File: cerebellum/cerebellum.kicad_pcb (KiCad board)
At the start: 4 copper layers, 91.5 x 52 mm, 82 parts, among them J1 PowerIn, J2 UART, J3 SWD_DBG, J4 SWD_DBG_PIN, J5 PowerOut, J6 CAN, Q1 AP2300, U1 OK1061-S, U2 TPS5430DDA, U3 BMI088, U4 TJA1042T, U5 ICP-20100, U6 TJA1042T, U7 TPS54231

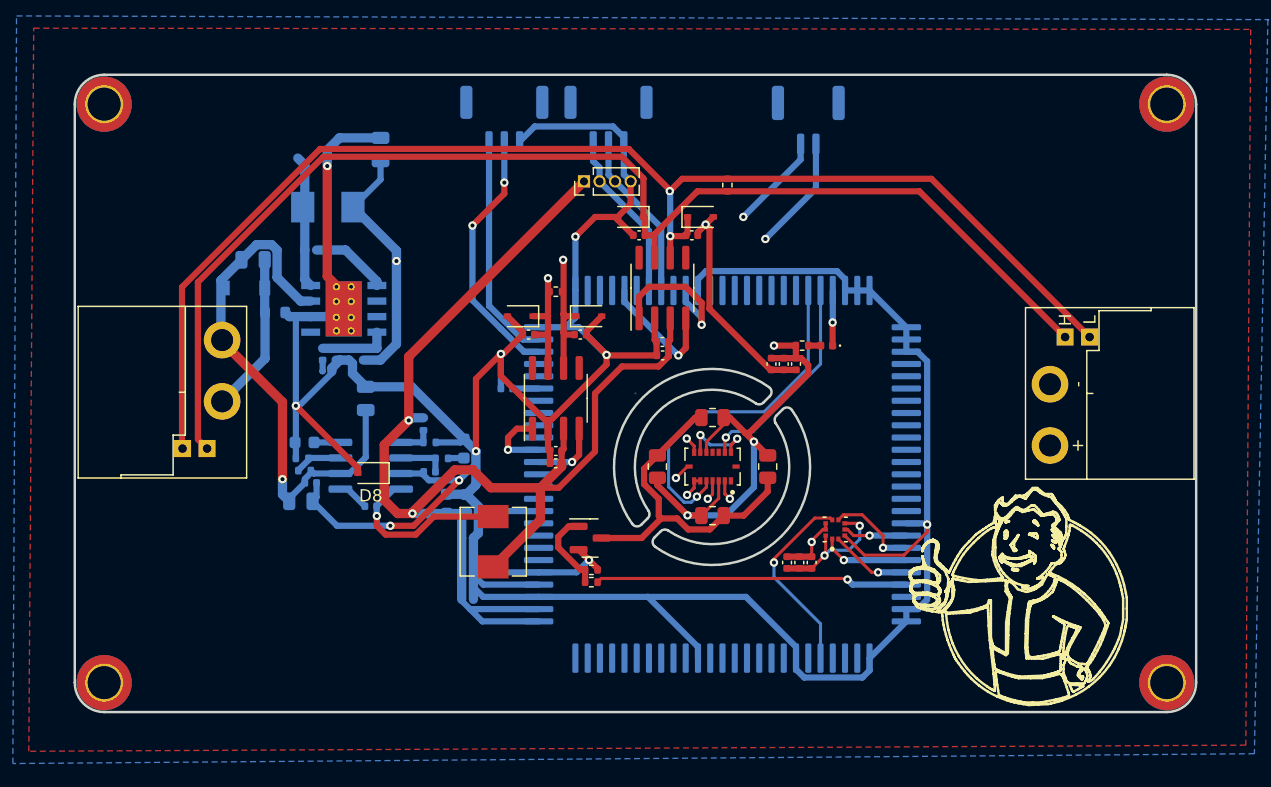
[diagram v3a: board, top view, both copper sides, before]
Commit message: [New] Rerouting cerebellum & add dxfs
1. Rerouting cerebellum for new design. There are only two layers in this design.
2. Add common board DXF file and cerebellum DXF file. Also I added their source file for convenient modification in the future.
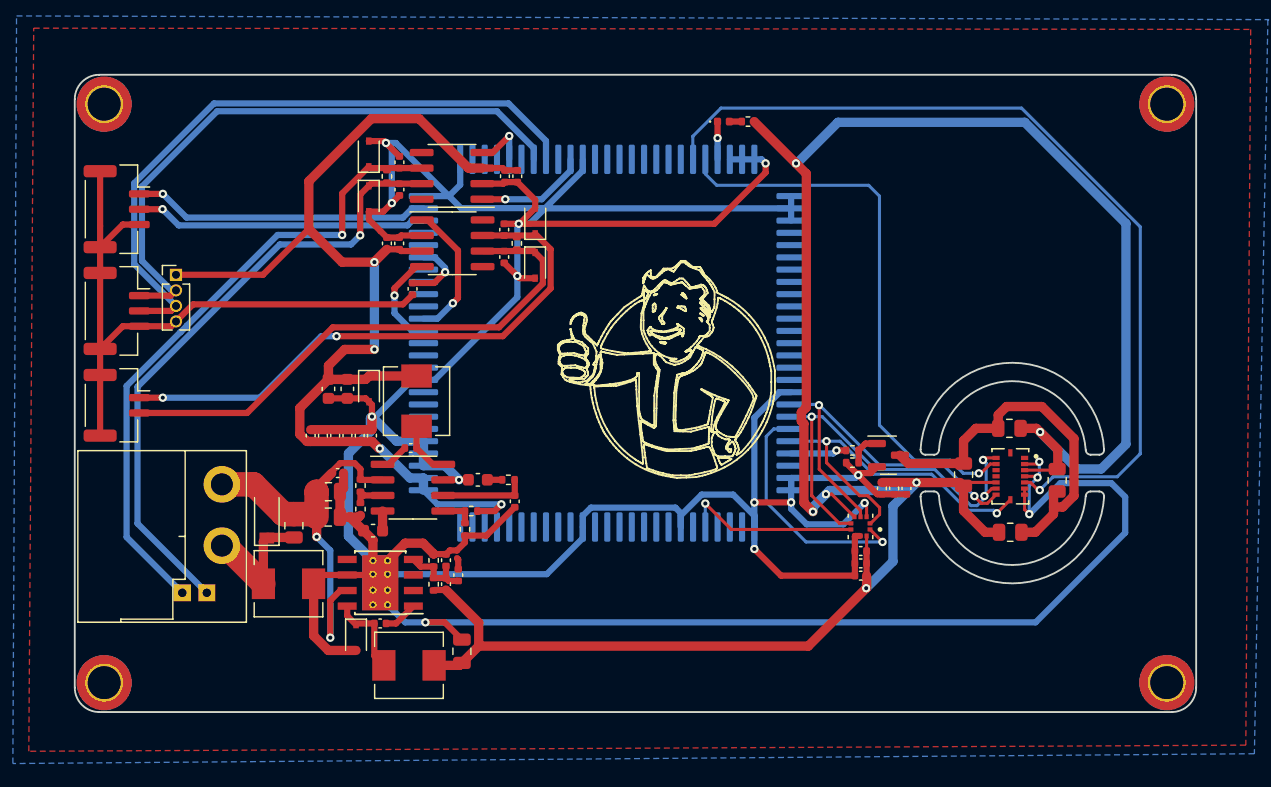
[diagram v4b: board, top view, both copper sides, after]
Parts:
- removed FB1: 220R, Resistor_SMD:R_0603_1608Metric
- removed J5: PowerOut, Rolling_Custom:XT30PW(2+2)
- added L3: 15uh, SLO0530H150MTT, Inductor_SMD:L_Sunlord_MWSA0518_5.4x5.2mm, F.Cu at (121.7, 115.5)
- C1, C13, C14, C15, C16, C17, C18, C19, C2, C21, C24, C25, C26, C27, C28, C3, C33, C36, C38, C4, C5, C6, D1, D2, J2, J4, L2, R11, R16, R17, R3, R4, R5, R6, R7, U2, U7: moved to F.Cu
- J6: footprint Connector_JST:JST_GH_BM02B-GHS-TBT_1x02-1MP_P1.25mm_Vertical -> Connector_JST:JST_GH_SM02B-GHS-TB_1x02-1MP_P1.25mm_Horizontal; moved to F.Cu
- moved J1 68.6 mm to (116.3, 111.7), turned to -90 degrees
- moved J6 61.0 mm to (107.7, 101.0), turned to -90 degrees
- moved J4 43.1 mm to (107.7, 93.3), turned to -90 degrees
- moved C19 41.5 mm to (135.8, 121.0)
- moved D2 39.3 mm to (127.2, 119.9), turned to -90 degrees
- moved L2 38.0 mm to (131.5, 122.2)
- moved J3 34.2 mm to (112.5, 90.3), turned to 0 degrees
- moved J2 32.5 mm to (107.7, 85.0), turned to -90 degrees
- moved C17 31.0 mm to (129.2, 118.8)
- moved R12 28.9 mm to (180.5, 102.8), turned to 180 degrees
- moved R13 28.3 mm to (184.4, 107.1), turned to -90 degrees
- moved R2 27.8 mm to (129.7, 82.3)
- moved D6 27.5 mm to (128.2, 80.5), turned to 90 degrees
- moved R14 26.0 mm to (180.6, 111.3), turned to 0 degrees
- moved Q1 25.3 mm to (170.6, 105.0)
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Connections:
- J2 pad MP: (no net) -> GND
- J4 pad MP: (no net) -> GND
- J6 pad MP: (no net) -> GND
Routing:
- net +24V: track 149.8 -> 32.8 mm, vias 1 -> 2
- net GNDA: track 107.0 -> 10.7 mm
- net +3V3: track 128.5 -> 188.1 mm
- net GND: track 378.8 -> 435.7 mm, vias 15 -> 16
- net CANFD_L: track 107.2 -> 52.3 mm, vias 2 -> 1
- net CANFD_H: track 102.4 -> 51.2 mm, vias 0 -> 1
- net GYRO_SCS: track 28.3 -> 72.8 mm
- net SWCLK: track 13.9 -> 53.7 mm
- net SWDIO: track 14.0 -> 49.7 mm
- net ACC_SCS: track 17.5 -> 46.3 mm
- net BMI_HEAT: track 25.5 -> 4.59 mm
- net +5V: track 108.1 -> 94.8 mm, vias 2 -> 4
- net ICP_SCS: track 7.21 -> 19.9 mm
- net Net-(C27-Pad1): track 14.6 -> 4.50 mm, vias 1 -> 0
- net CAN_L: track 34.9 -> 44.4 mm, vias 2 -> 0
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- removed copper zone on In1.Cu, net +3V3
- removed copper zone on In2.Cu, net +5V
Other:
- outline, holes or cut-outs redrawn
- copper layers 4 -> 2

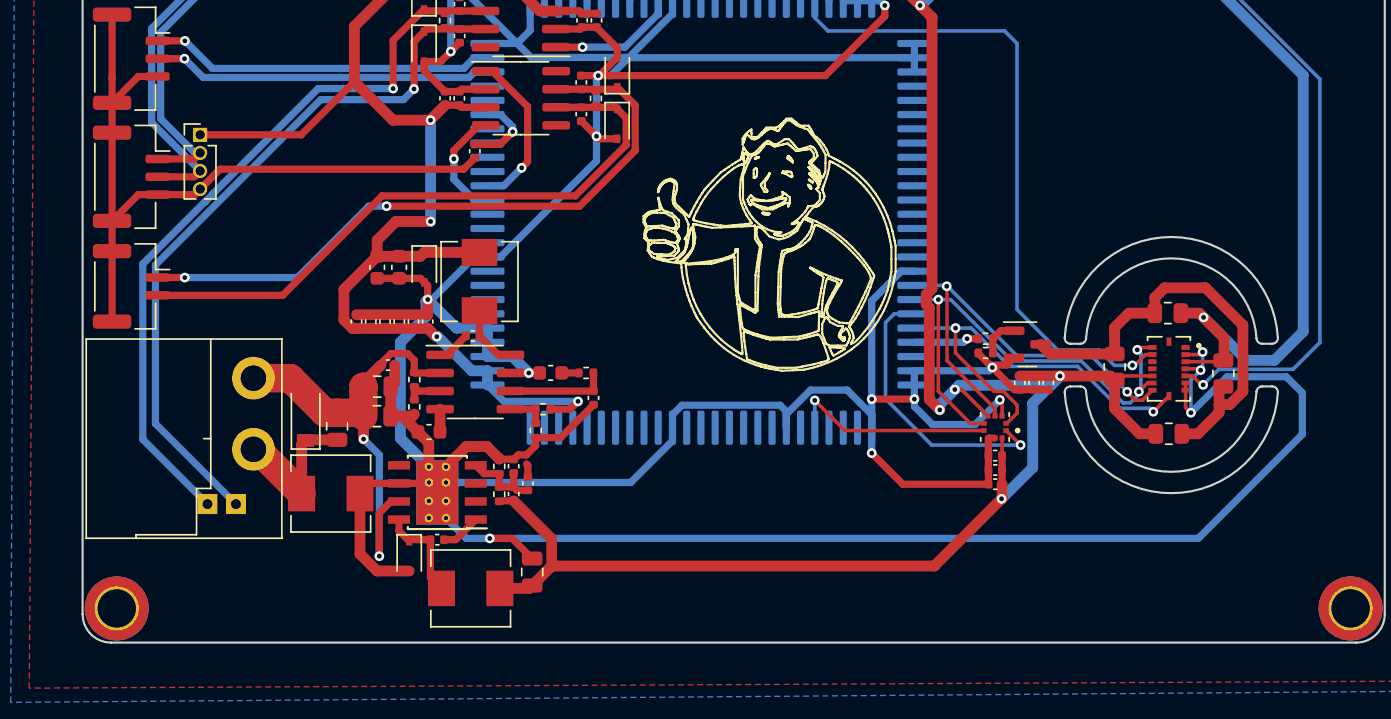
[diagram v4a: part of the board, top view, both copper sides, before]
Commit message: [Modify] Change XT30(2+2) input to XT30 + GH 2pin
As commit before.
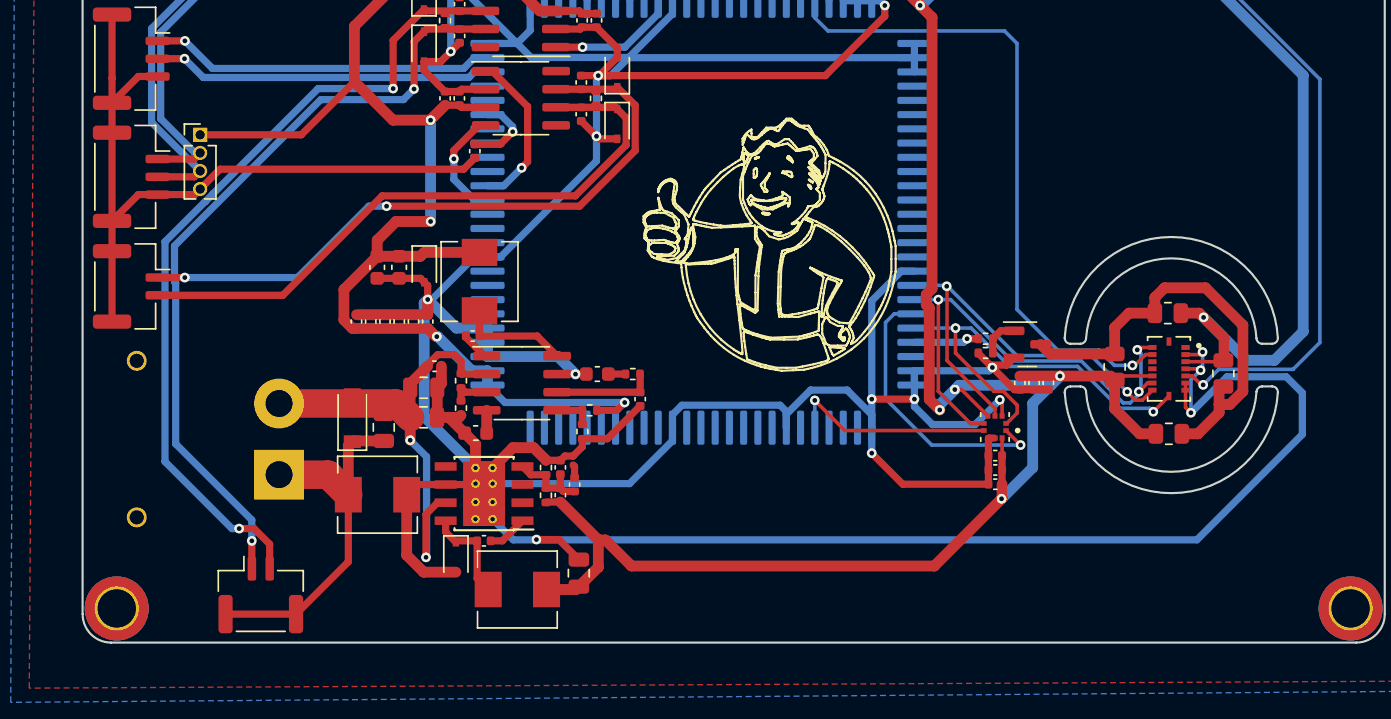
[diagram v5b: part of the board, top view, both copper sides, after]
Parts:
- added J5: CAN FD, Connector_JST:JST_GH_SM02B-GHS-TB_1x02-1MP_P1.25mm_Horizontal, F.Cu at (116.8, 122.7)
- J1: footprint Rolling_Custom:XT30PW(2+2) -> Connector_AMASS:AMASS_XT30PW-M_1x02_P2.50mm_Horizontal; moved to B.Cu
- moved C13 3.28 mm to (125.4, 110.9)
- moved C14 3.28 mm to (143.4, 108.9)
- moved C15 3.28 mm to (140.4, 107.1)
- moved C16 3.28 mm to (128.2, 110.2)
- moved C17 3.28 mm to (132.4, 118.8)
- moved C18 3.28 mm to (128.2, 108.1)
- moved C19 3.28 mm to (139.1, 121.1)
- moved C21 3.28 mm to (137.8, 115.6)
- moved C24 3.28 mm to (138.8, 114.9)
- moved C26 3.28 mm to (131.9, 111.3)
- moved C28 3.28 mm to (137.8, 113.7)
- moved D1 3.28 mm to (123.2, 110.2)
- moved L2 3.28 mm to (134.8, 122.3)
- moved L3 3.28 mm to (125.0, 115.6)
- moved R11 3.28 mm to (138.7, 113.2)
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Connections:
- J1 pad 1: +24V -> GNDA
- J1 pad 2: GNDA -> +24V
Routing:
- net GNDA: track 10.7 -> 26.4 mm
- net CANFD_L: track 52.3 -> 58.2 mm, vias 1 -> 2
- net CANFD_H: track 51.2 -> 55.0 mm, vias 1 -> 2
- net +5V: track 94.8 -> 98.1 mm
- net Net-(C27-Pad1): track 4.50 -> 7.82 mm
- net GND: track 435.7 -> 432.6 mm
- net +3V3: track 188.1 -> 185.6 mm
- net +24V: track 32.8 -> 34.0 mm

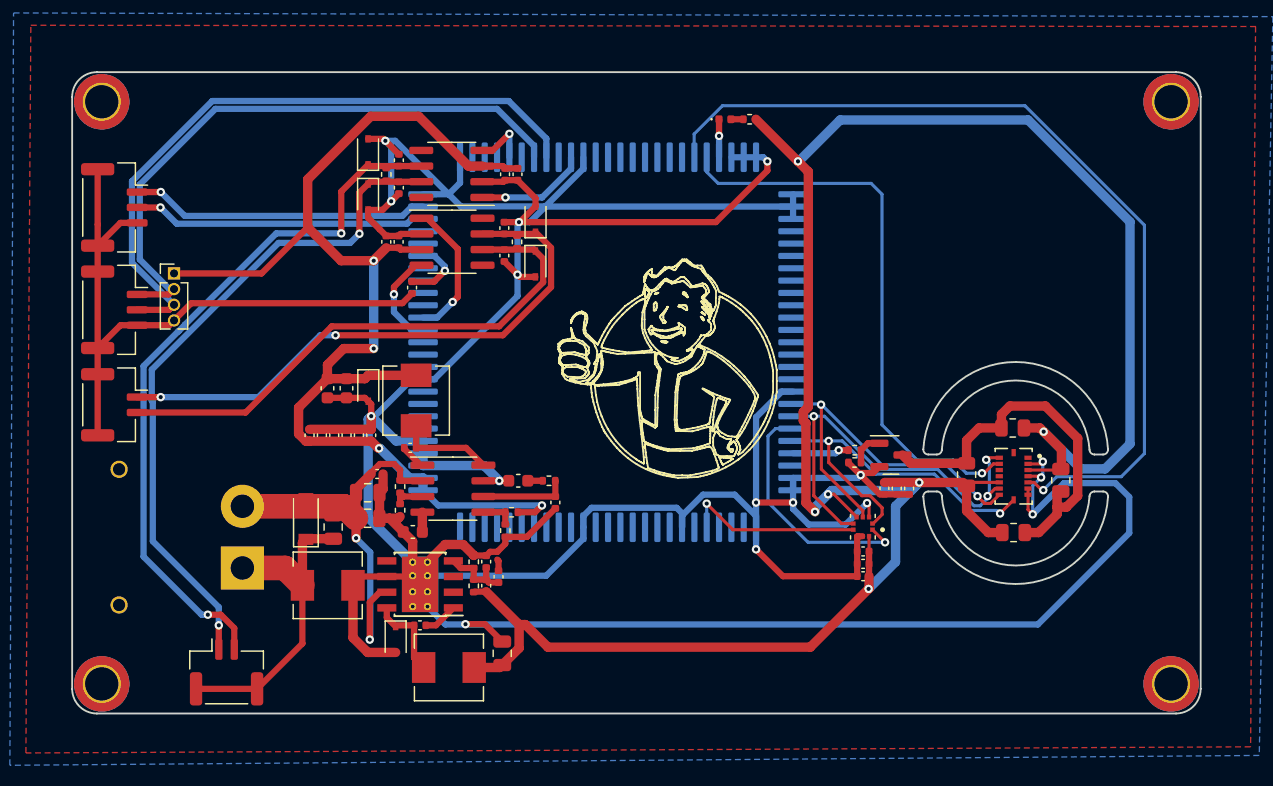
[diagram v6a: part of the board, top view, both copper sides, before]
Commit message: [Fix] Correct mounting hole positions
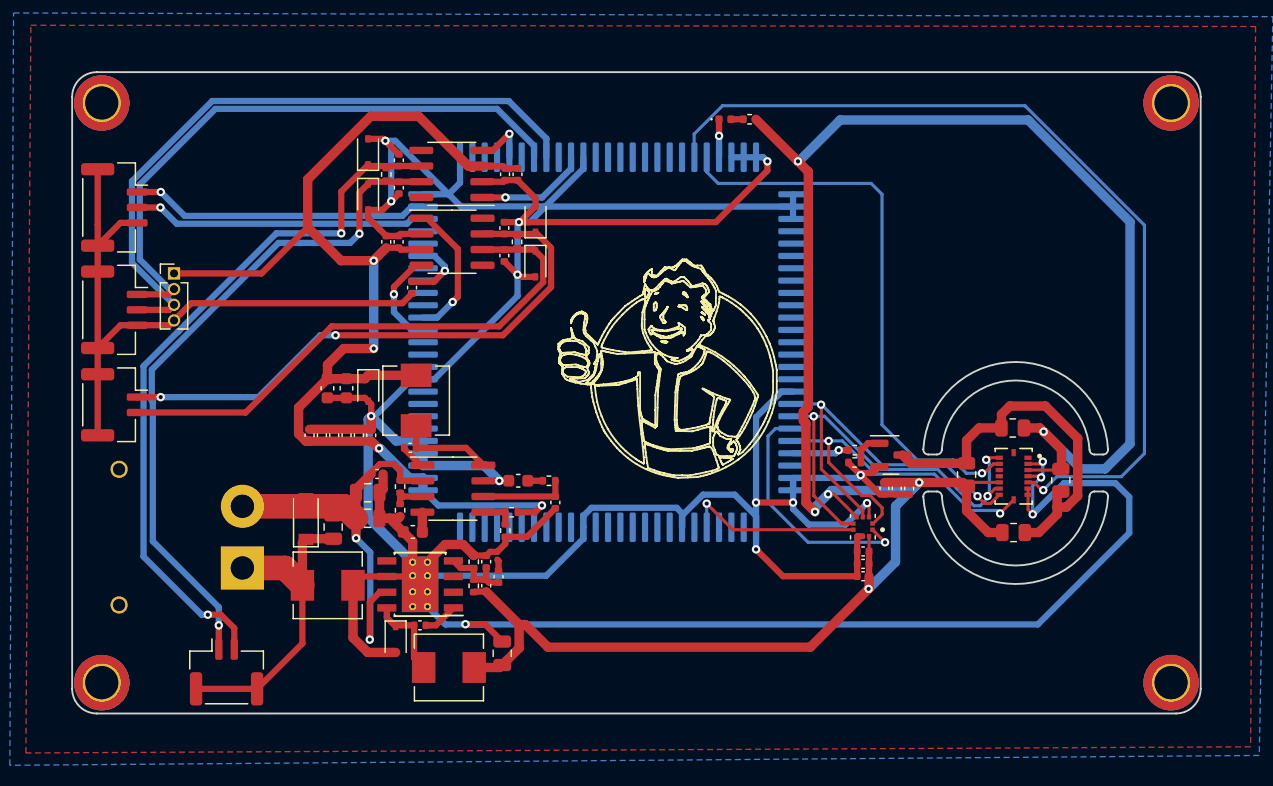
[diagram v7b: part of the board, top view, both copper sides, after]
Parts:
- moved Mount1 0.10 mm to (106.7, 76.5)
- moved Mount2 0.10 mm to (193.3, 76.5)
- moved Mount3 0.10 mm to (193.3, 123.5)
- moved Mount4 0.10 mm to (106.7, 123.5)
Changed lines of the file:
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@@
   )
   (footprint "MountingHole:MountingHole_2.7mm_M2.5_ISO7380_Pad_TopBottom" (layer "F.Cu")
-    (at 106.65 76.4)
+    (at 106.65 76.5)
     (descr "Mounting Hole 2.7mm, M2.5, ISO7380")
     (tags "mounting hole 2.7mm m2.5 iso7380")
@@
   )
   (footprint "MountingHole:MountingHole_2.7mm_M2.5_ISO7380_Pad_TopBottom" (layer "F.Cu")
-    (at 106.65 123.6)
+    (at 106.65 123.5)
     (descr "Mounting Hole 2.7mm, M2.5, ISO7380")
     (tags "mounting hole 2.7mm m2.5 iso7380")
@@
   )
   (footprint "MountingHole:MountingHole_2.7mm_M2.5_ISO7380_Pad_TopBottom" (layer "F.Cu")
-    (at 193.35 123.6)
+    (at 193.35 123.5)
     (descr "Mounting Hole 2.7mm, M2.5, ISO7380")
     (tags "mounting hole 2.7mm m2.5 iso7380")
@@
   )
   (footprint "MountingHole:MountingHole_2.7mm_M2.5_ISO7380_Pad_TopBottom" (layer "F.Cu")
-    (at 193.35 76.4)
+    (at 193.35 76.5)
     (descr "Mounting Hole 2.7mm, M2.5, ISO7380")
     (tags "mounting hole 2.7mm m2.5 iso7380")

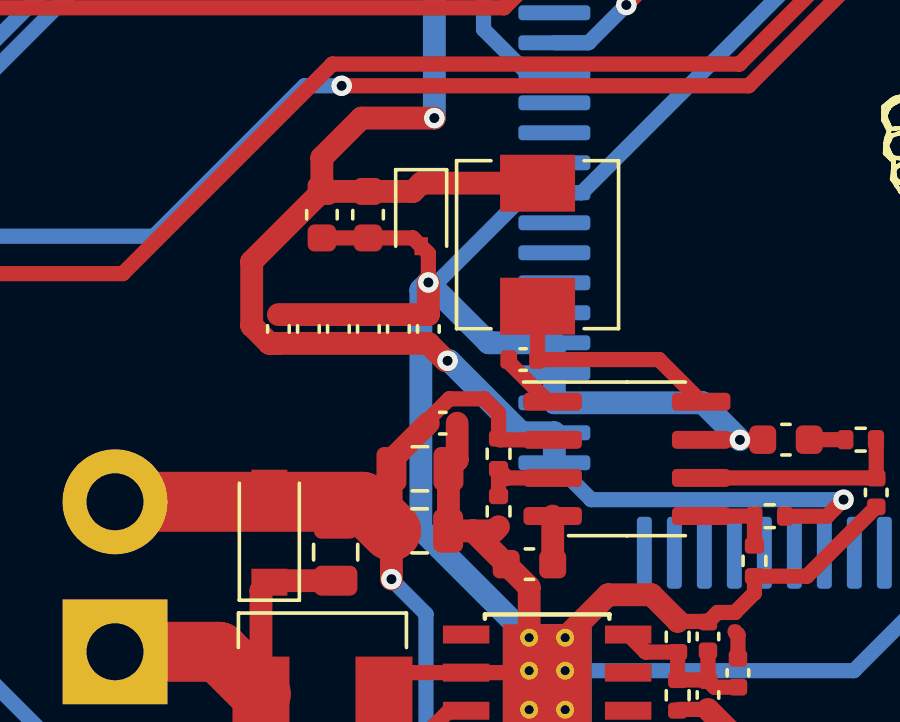
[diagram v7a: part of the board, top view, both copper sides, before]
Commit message: [Fix] Correct capacities in 24Vto5V converter
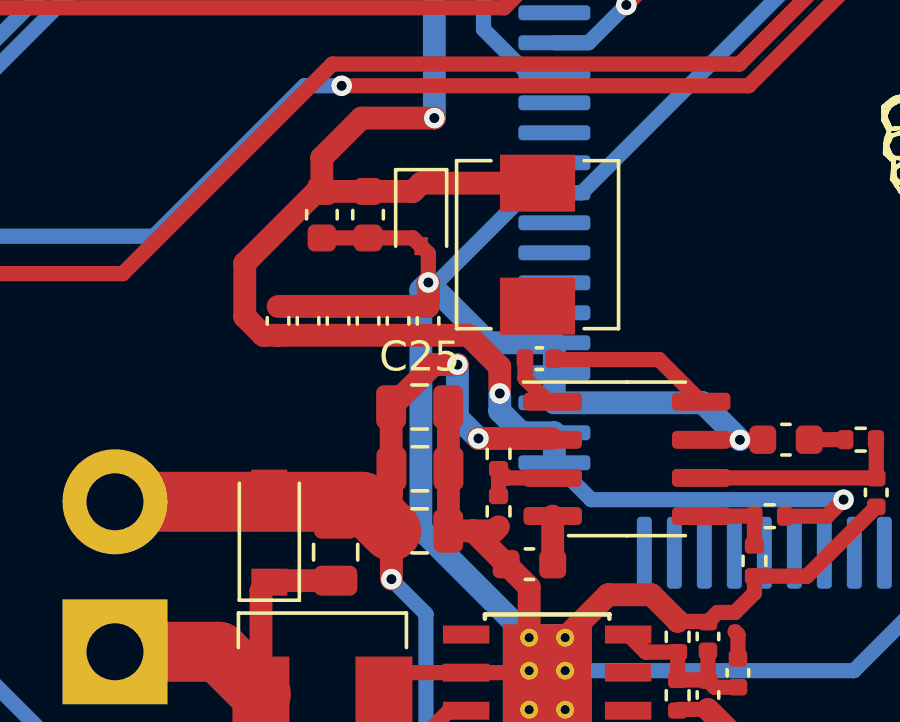
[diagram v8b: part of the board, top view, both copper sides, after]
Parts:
- C1, C10, C2, C27, C30, C32, C38, C5, C51, C7: value 100nF, 10%, 10V -> 100nF/10V/0402
- C11, C22, C23, C9: value 100pF, 10%, 10V -> 100pF/1%/50V/0402
- C12, C29, C3, C31, C8: value 4.7uF, 10%, 10V -> 4.7uF/10V/0402
- C13, C16, C18: value 4.7uF 50V -> 4.7uF/50V/0805
- C14: value 10pf 50V -> 10pf/50V/0402
- C15: value 1.5nf 50V -> 1.5nf/50V/0603
- C17: value 10nf 50V -> 10nf/50V/0402
- C19: value 100uf 50V -> 100uf/50V/0805
- C20: value 100nf 10V -> 100nf/10V/0402
- C21: value 1.5nf 50V -> 1.5nf/50V/0402
- C24: value 100nf 50V -> 100nf/50V/0402
- C25: value 10uf 50V -> 10uf/50V/0805; footprint Capacitor_SMD:C_0402_1005Metric -> Capacitor_SMD:C_0805_2012Metric
- C26: value 8.2nf 50V -> 8.2nf/50V/0603
- C28: value 150pf 50V -> 150pf/50V/0402
- C33, C36: value 47uf 50V -> 47uf/50V/0603
- C4: value 1uF, 10%, 10V -> 1uF/10V/0402
- C6: value 10uF, 10%, 10V -> 10uF/10V/0402
- D5: value LTST-C281KFKT-5A -> LTST-C281KFKT-5A/0402
- L1, L2, L3: value 15uh, SLO0530H150MTT -> 15uh/SLO0530H150MTT
- R1: value 1k -> 1k/0402
- R10, R6: value 10k -> 10k/0402
- R11: value 549R -> 549R/0201
- R12, R13, R14, R15: value 33R/1% -> 33R/1%/0805
- R16: value 10.2k -> 10.2k/0402
- R17: value 1.96k -> 1.96k/0402
- R2, R8: value 120R -> 120R/0402
- R3: value 64.9k -> 64.9k/0402
- R4: value 169k -> 169k/0402
- R5: value 20.5 -> 20.5k/0402
- R7: value 5.9k -> 5.9k/0402
- R9: value 100R -> 100R/0402
- moved C25 0.94 mm to (128.2, 106.0)
- moved C27 0.54 mm to (132.2, 104.4)
- moved C1 0.27 mm to (125.5, 103.2)
- moved C2 0.27 mm to (124.5, 103.2)
- moved C3 0.27 mm to (126.5, 103.2)
- moved C4 0.27 mm to (127.5, 103.2)
- moved C6 0.27 mm to (123.5, 103.2)
- moved C5 0.27 mm to (128.5, 103.2)
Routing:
- net +24V: track 34.0 -> 37.7 mm, vias 2 -> 4
- net Net-(C27-Pad1): track 7.82 -> 5.51 mm
- net +5V: track 98.1 -> 99.2 mm
